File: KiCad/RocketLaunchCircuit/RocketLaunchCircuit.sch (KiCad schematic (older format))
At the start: 36 parts, among them J1 Arduino_GPIO, J10 LogicConverter_BiDirectional, J11 ConnectorTarget3, J12 ConnectorTarget4, J13 ExternalGameControlIO, J14 Dupont_3Pin_Female, J15 Screw_Terminal_01x02, J2 Arduino_Serial_And_5V, J3 MicroBit_40PinExtender, J4 ConnectorTarget1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

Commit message: Created a custom symbol for the bi-directional logic converter module
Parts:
- removed J10, J8: LogicConverter_BiDirectional, symbol Connector_Generic:Conn_02x06_Row_Letter_Last
- added U1, U2: Bi-Directional_logic_shifter, symbol RocketLaunch_Library:Bi-Directional_logic_shifter
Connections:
- wire segments 195 -> 199
- no-connect marks 0 -> 15
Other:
- note added: "Notch of the IDC connectors (see list) on this side:\n- Arduino_GPIO\n- Arduino_Serial_and_5V\n- MicroBit_40PinExtender"
- moved on the sheet: C5, C6, C7, C8, J13, J3, R5, R7, R8, R9

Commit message: Updated the names of the LedDataTargetx singals with the correct values for 'x'
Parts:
- C1, C2, C3, C4, C5, C6, C7, C8: symbol Device:C -> RocketLaunchCircuit-rescue:C-Device
- J1, J13: symbol Connector_Generic:Conn_02x05_Counter_Clockwise -> RocketLaunchCircuit-rescue:Conn_02x05_Counter_Clockwise-Connector_Generic
- J11, J12, J4, J7: symbol Connector_Generic:Conn_01x05 -> RocketLaunchCircuit-rescue:Conn_01x05-Connector_Generic
- J14, J9: symbol Connector_Generic:Conn_01x03 -> RocketLaunchCircuit-rescue:Conn_01x03-Connector_Generic
- J15: symbol Connector:Screw_Terminal_01x02 -> RocketLaunchCircuit-rescue:Screw_Terminal_01x02-Connector
- J2: symbol Connector_Generic:Conn_02x03_Counter_Clockwise -> RocketLaunchCircuit-rescue:Conn_02x03_Counter_Clockwise-Connector_Generic
- J3: symbol Connector_Generic:Conn_02x20_Row_Letter_Last -> RocketLaunchCircuit-rescue:Conn_02x20_Row_Letter_Last-Connector_Generic
- J5, J6: symbol Connector:USB_A -> RocketLaunchCircuit-rescue:USB_A-Connector
- R1, R2, R3, R4, R5, R7, R8, R9: symbol Device:R -> RocketLaunchCircuit-rescue:R-Device
- R6: symbol Device:R_Small -> RocketLaunchCircuit-rescue:R_Small-Device
- SW1: symbol Switch:SW_DPST_x2 -> RocketLaunchCircuit-rescue:SW_DPST_x2-Switch
- SW2, SW3: symbol Switch:SW_DPDT_x2 -> RocketLaunchCircuit-rescue:SW_DPDT_x2-Switch
- SW4: symbol Device:Rotary_Encoder_Switch -> RocketLaunchCircuit-rescue:Rotary_Encoder_Switch-Device
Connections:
- net LedDataTarget1_5V: no longer J11.3 (Pin_3), J12.3 (Pin_3), J7.3 (Pin_3)
- net LedDataTarget2_5V: now also J7.3 (Pin_3)
- net LedDataTarget3_5V: now also J11.3 (Pin_3)
- net LedDataTarget4_5V: now also J12.3 (Pin_3)
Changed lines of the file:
@@
 $EndDescr
 $Comp
-L Connector:Screw_Terminal_01x02 J15
+L RocketLaunchCircuit-rescue:Screw_Terminal_01x02-Connector J15
 U 1 1 5E6E483D
 P 6500 7150
@@
 $EndComp
 $Comp
-L Switch:SW_DPDT_x2 SW2
+L RocketLaunchCircuit-rescue:SW_DPDT_x2-Switch SW2
 U 1 1 5E6E85BB
 P 8500 2100
@@
 $EndComp
 $Comp
-L power:GND #PWR011
+L RocketLaunchCircuit-rescue:GND-power #PWR011
 U 1 1 5E707618
 P 2150 3300
@@
 5V_PowerSupply
 $Comp
-L Connector_Generic:Conn_01x03 J9
+L RocketLaunchCircuit-rescue:Conn_01x03-Connector_Generic J9
 U 1 1 5E6A9AF2
 P 4950 700
@@
 $EndComp
 $Comp
-L Connector_Generic:Conn_02x03_Counter_Clockwise J2
+L RocketLaunchCircuit-rescue:Conn_02x03_Counter_Clockwise-Connector_Generic J2
 U 1 1 5E6AB262
 P 3350 2300
@@
 $EndComp
 $Comp
-L Connector_Generic:Conn_02x05_Counter_Clockwise J1
+L RocketLaunchCircuit-rescue:Conn_02x05_Counter_Clockwise-Connector_Generic J1
 U 1 1 5E6AC440
 P 3500 1300
@@
 $EndComp
 $Comp
-L Connector_Generic:Conn_02x20_Row_Letter_Last J3
+L RocketLaunchCircuit-rescue:Conn_02x20_Row_Letter_Last-Connector_Generic J3
 U 1 1 5E6AC8BC
 P 3200 4950
@@
 	8300 2000 7950 2000
 $Comp
-L power:GND #PWR017
+L RocketLaunchCircuit-rescue:GND-power #PWR017
 U 1 1 5E6AFC6B
 P 8050 2200
@@
 PlayerCountSignal
 $Comp
-L Switch:SW_DPDT_x2 SW3
+L RocketLaunchCircuit-rescue:SW_DPDT_x2-Switch SW3
 U 1 1 5E6B920E
 P 8500 2850
@@
 	8300 2750 7950 2750
 $Comp
-L power:GND #PWR018
+L RocketLaunchCircuit-rescue:GND-power #PWR018
 U 1 1 5E6B9215
 P 8050 2950
@@
 LedMatrixData
 $Comp
-L power:GND #PWR07
+L RocketLaunchCircuit-rescue:GND-power #PWR07
 U 1 1 5E6CDC4C
 P 5050 1300
@@
 5V_PowerSupply
 $Comp
-L power:GND #PWR019
+L RocketLaunchCircuit-rescue:GND-power #PWR019
 U 1 1 5E73009E
 P 6300 6800
@@
 MicroBit_P16
 $Comp
-L power:GND #PWR021
+L RocketLaunchCircuit-rescue:GND-power #PWR021
 U 1 1 5E98B09B
 P 3500 4150
@@
 Arduino_5V
 $Comp
-L power:GND #PWR022
+L RocketLaunchCircuit-rescue:GND-power #PWR022
 U 1 1 5EBDEE77
 P 3700 2400
@@
 StartResetSignal
 $Comp
-L power:GND #PWR016
+L RocketLaunchCircuit-rescue:GND-power #PWR016
 U 1 1 5ED7A6E1
 P 8650 3450
@@
 $EndComp
 $Comp
-L Switch:SW_DPST_x2 SW1
+L RocketLaunchCircuit-rescue:SW_DPST_x2-Switch SW1
 U 1 1 5E6EA688
 P 8400 3450
@@
 	2100 3300 2150 3300
 $Comp
-L Connector:USB_A J5
+L RocketLaunchCircuit-rescue:USB_A-Connector J5
 U 1 1 5E70F829
 P 2100 2900
@@
 $EndComp
 $Comp
-L power:GND #PWR012
+L RocketLaunchCircuit-rescue:GND-power #PWR012
 U 1 1 5E77BF6C
 P 2750 3900
@@
 	2700 3900 2750 3900
 $Comp
-L Connector:USB_A J6
+L RocketLaunchCircuit-rescue:USB_A-Connector J6
 U 1 1 5E77BF75
 P 2700 3500
@@
 	3500 4050 3500 4150
 $Comp
-L Connector_Generic:Conn_01x05 J4
+L RocketLaunchCircuit-rescue:Conn_01x05-Connector_Generic J4
 U 1 1 5E7ECC5B
 P 2450 7150
@@
 $EndComp
 $Comp
-L power:GND #PWR02
+L RocketLaunchCircuit-rescue:GND-power #PWR02
 U 1 1 5E7EF8C8
 P 2750 6850
@@
 LedDataTarget1_5V
 $Comp
-L Device:R R1
+L RocketLaunchCircuit-rescue:R-Device R1
 U 1 1 5E7EF8D4
 P 2300 6500
@@
 $EndComp
 $Comp
-L Device:C C1
+L RocketLaunchCircuit-rescue:C-Device C1
 U 1 1 5E7EF8DA
 P 2050 6500
@@
 SwitchTarget1
 $Comp
-L power:GND #PWR01
+L RocketLaunchCircuit-rescue:GND-power #PWR01
 U 1 1 5E80F09C
 P 2100 6650
@@
 SizeTarget1
 $Comp
-L Connector_Generic:Conn_01x05 J7
+L RocketLaunchCircuit-rescue:Conn_01x05-Connector_Generic J7
 U 1 1 5E87FD51
 P 3500 7150
@@
 $EndComp
 $Comp
-L power:GND #PWR06
+L RocketLaunchCircuit-rescue:GND-power #PWR06
 U 1 1 5E87FD57
 P 3800 6850
@@
 	3500 6950 3500 6250
 Text Label 3500 6250 3    50   ~ 0
-LedDataTarget1_5V
-$Comp
-L Device:R R2
+LedDataTarget2_5V
+$Comp
+L RocketLaunchCircuit-rescue:R-Device R2
 U 1 1 5E87FD63
 P 3350 6500
@@
 $EndComp
 $Comp
-L Device:C C2
+L RocketLaunchCircuit-rescue:C-Device C2
 U 1 1 5E87FD69
 P 3100 6500
@@
 SwitchTarget2
 $Comp
-L power:GND #PWR03
+L RocketLaunchCircuit-rescue:GND-power #PWR03
 U 1 1 5E87FD71
 P 3150 6650
@@
 SizeTarget2
 $Comp
-L Connector_Generic:Conn_01x05 J11
+L RocketLaunchCircuit-rescue:Conn_01x05-Connector_Generic J11
 U 1 1 5E88B164
 P 4550 7150
@@
 $EndComp
 $Comp
-L power:GND #PWR013
+L RocketLaunchCircuit-rescue:GND-power #PWR013
 U 1 1 5E88B16A
 P 4850 6850
@@
 	4550 6950 4550 6250
 Text Label 4550 6250 3    50   ~ 0
-LedDataTarget1_5V
-$Comp
-L Device:R R3
+LedDataTarget3_5V
+$Comp
+L RocketLaunchCircuit-rescue:R-Device R3
 U 1 1 5E88B176
 P 4400 6500
@@
 $EndComp
 $Comp
-L Device:C C3
+L RocketLaunchCircuit-rescue:C-Device C3
 U 1 1 5E88B17C
 P 4150 6500
@@
 SwitchTarget3
 $Comp
-L power:GND #PWR010
+L RocketLaunchCircuit-rescue:GND-power #PWR010
 U 1 1 5E88B184
 P 4200 6650
@@
 SizeTarget3
 $Comp
-L Connector_Generic:Conn_01x05 J12
+L RocketLaunchCircuit-rescue:Conn_01x05-Connector_Generic J12
 U 1 1 5E897B46
 P 5600 7150
@@
 $EndComp
 $Comp
-L power:GND #PWR015
+L RocketLaunchCircuit-rescue:GND-power #PWR015
 U 1 1 5E897B4C
 P 5900 6850
@@
 	5600 6950 5600 6250
 Text Label 5600 6250 3    50   ~ 0
-LedDataTarget1_5V
-$Comp
-L Device:R R4
+LedDataTarget4_5V
+$Comp
+L RocketLaunchCircuit-rescue:R-Device R4
 U 1 1 5E897B58
 P 5450 6500
@@
 $EndComp
 $Comp
-L Device:C C4
+L RocketLaunchCircuit-rescue:C-Device C4
 U 1 1 5E897B5E
 P 5200 6500
@@
 SwitchTarget4
 $Comp
-L power:GND #PWR014
+L RocketLaunchCircuit-rescue:GND-power #PWR014
 U 1 1 5E897B66
 P 5250 6650
@@
 SizeTarget4
 $Comp
-L power:GND #PWR024
+L RocketLaunchCircuit-rescue:GND-power #PWR024
 U 1 1 5E8F3D2E
 P 8000 1400
@@
 PointSelectorEncoderB
 $Comp
-L power:GND #PWR025
+L RocketLaunchCircuit-rescue:GND-power #PWR025
 U 1 1 5E942130
 P 8700 1500
@@
 $EndComp
 $Comp
-L Device:Rotary_Encoder_Switch SW4
+L RocketLaunchCircuit-rescue:Rotary_Encoder_Switch-Device SW4
 U 1 1 5E8F157E
 P 8350 1400
@@
 	5600 1600 6000 1600
 $Comp
-L power:GND #PWR023
+L RocketLaunchCircuit-rescue:GND-power #PWR023
 U 1 1 5EB8702E
 P 5850 1900
@@
 	8750 2650 8750 2850
 $Comp
-L Connector_Generic:Conn_01x03 J14
+L RocketLaunchCircuit-rescue:Conn_01x03-Connector_Generic J14
 U 1 1 5EB538A7
 P 6200 1700
@@
 $EndComp
 $Comp
-L Device:R_Small R6
+L RocketLaunchCircuit-rescue:R_Small-Device R6
 U 1 1 5EB9F373
 P 5850 1800
@@
 	5200 3250 5200 3300
 $Comp
-L power:GND #PWR04
+L RocketLaunchCircuit-rescue:GND-power #PWR04
 U 1 1 5EA19618
 P 5300 3250
@@
 	5300 3250 5300 3300
 $Comp
-L power:GND #PWR05
+L RocketLaunchCircuit-rescue:GND-power #PWR05
 U 1 1 5EA3BCA6
 P 5300 4350
@@
 	5600 4700 5600 4750
 $Comp
-L power:GND #PWR08
+L RocketLaunchCircuit-rescue:GND-power #PWR08
 U 1 1 5EB84976
 P 5700 4700
@@
 	5700 4700 5700 4750
 $Comp
-L power:GND #PWR09
+L RocketLaunchCircuit-rescue:GND-power #PWR09
 U 1 1 5EB94E6F
 P 5700 5800
@@
 	4450 2750 4800 2750
 $Comp
-L Device:C C6
+L RocketLaunchCircuit-rescue:C-Device C6
 U 1 1 5EDDB888
 P 4450 2600
@@
 	4650 2950 4800 2950
 $Comp
-L Device:C C7
+L RocketLaunchCircuit-rescue:C-Device C7
 U 1 1 5ED5AEFD
 P 4550 2700
@@
 $EndComp
 $Comp
-L Device:C C8
+L RocketLaunchCircuit-rescue:C-Device C8
 U 1 1 5ED22825
 P 4650 2800
@@
 	6000 2750 6750 2750
 $Comp
-L Device:R R9
+L RocketLaunchCircuit-rescue:R-Device R9
 U 1 1 5ECBAF3A
 P 4950 2950
@@
 $EndComp
 $Comp
-L Device:R R8
+L RocketLaunchCircuit-rescue:R-Device R8
 U 1 1 5ECACC72
 P 4950 2850
@@
 $EndComp
 $Comp
-L Device:R R7
+L RocketLaunchCircuit-rescue:R-Device R7
 U 1 1 5EC9E8CF
 P 4950 2750
@@
 	5650 2950 6600 2950
 $Comp
-L power:GND #PWR020
+L RocketLaunchCircuit-rescue:GND-power #PWR020
 U 1 1 5E8DAE92
 P 6150 2450
@@
 $EndComp
 $Comp
-L Connector_Generic:Conn_02x05_Counter_Clockwise J13
+L RocketLaunchCircuit-rescue:Conn_02x05_Counter_Clockwise-Connector_Generic J13
 U 1 1 5E8CF06C
 P 5350 2750
@@
 $EndComp
 $Comp
-L Device:C C5
+L RocketLaunchCircuit-rescue:C-Device C5
 U 1 1 5ED5FABC
 P 6000 2600
@@
 $EndComp
 $Comp
-L Device:R R5
+L RocketLaunchCircuit-rescue:R-Device R5
 U 1 1 5ED5FAB6
 P 5850 2750

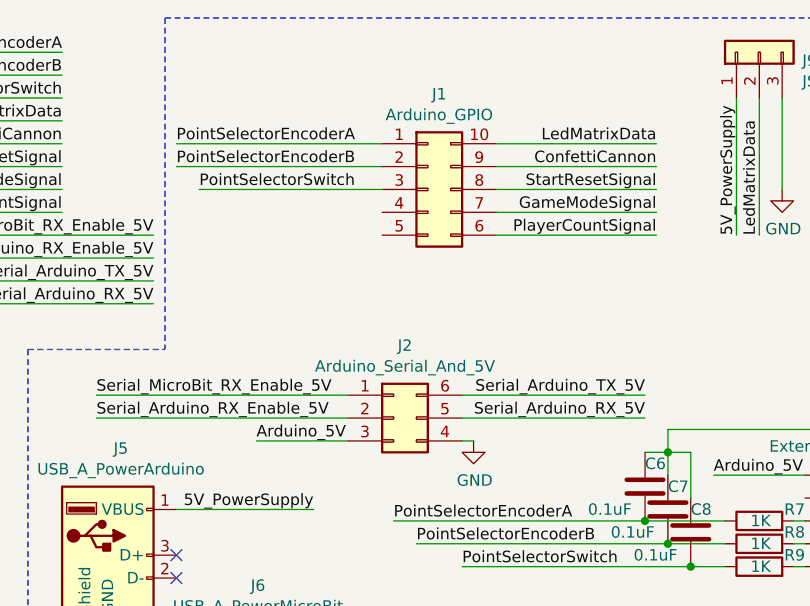
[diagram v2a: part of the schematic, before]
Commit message: Updated the connector pin layout for the idc connectors between the arduino and the perfboard
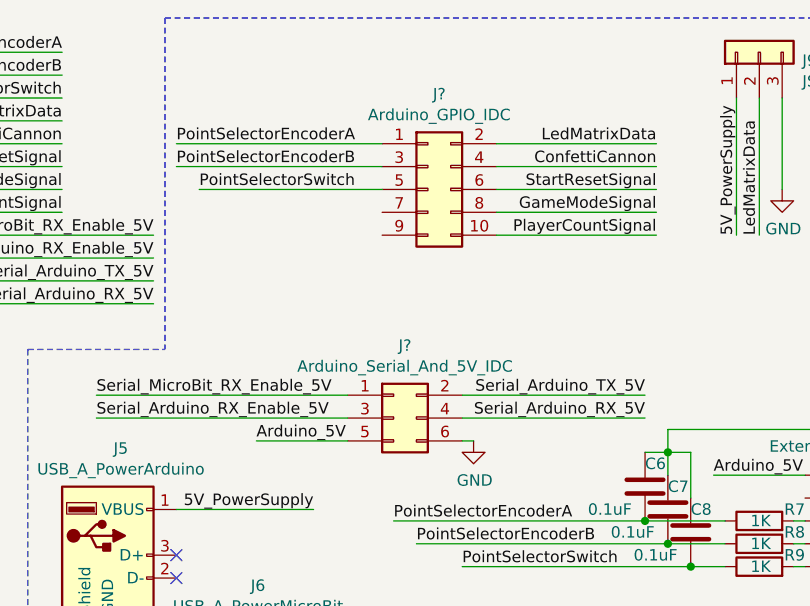
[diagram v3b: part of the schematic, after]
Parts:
- removed J1: Arduino_GPIO, symbol RocketLaunchCircuit-rescue:Conn_02x05_Counter_Clockwise-Connector_Generic
- removed J2: Arduino_Serial_And_5V, symbol RocketLaunchCircuit-rescue:Conn_02x03_Counter_Clockwise-Connector_Generic
- added J?: Arduino_GPIO_IDC, symbol Connector_Generic:Conn_02x05_Odd_Even
- added J?: Arduino_Serial_And_5V_IDC, symbol Connector_Generic:Conn_02x03_Odd_Even
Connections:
- net Arduino_5V: now also J?.5 (Pin_5)
- net Arduino_P0: now also J?.4 (Pin_4)
- net Arduino_P1: now also J?.2 (Pin_2)
- net Arduino_P10: now also J?.3 (Pin_3)
- net Arduino_P11: now also J?.1 (Pin_1)
- net Arduino_P2: now also J?.3 (Pin_3)
- net Arduino_P3: now also J?.1 (Pin_1)
- net Arduino_P4: now also J?.10 (Pin_10)
- net Arduino_P5: now also J?.8 (Pin_8)
- net Arduino_P6: now also J?.6 (Pin_6)
- net Arduino_P7: now also J?.4 (Pin_4)
- net Arduino_P8: now also J?.2 (Pin_2)
- net Arduino_P9: now also J?.5 (Pin_5)
- net GND: now also J?.6 (Pin_6)
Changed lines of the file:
@@
-$EndComp
-$Comp
-L RocketLaunchCircuit-rescue:Conn_02x03_Counter_Clockwise-Connector_Generic J2
-U 1 1 5E6AB262
-P 3350 2300
-F 0 "J2" H 3400 2617 50  0000 C CNN
-F 1 "Arduino_Serial_And_5V" H 3400 2526 50  0000 C CNN
-F 2 "" H 3350 2300 50  0001 C CNN
-F 3 "~" H 3350 2300 50  0001 C CNN
-	1    3350 2300
-	1    0    0    -1
-$EndComp
-$Comp
-L RocketLaunchCircuit-rescue:Conn_02x05_Counter_Clockwise-Connector_Generic J1
-U 1 1 5E6AC440
-P 3500 1300
-F 0 "J1" H 3550 1717 50  0000 C CNN
-F 1 "Arduino_GPIO" H 3550 1626 50  0000 C CNN
-F 2 "" H 3500 1300 50  0001 C CNN
-F 3 "~" H 3500 1300 50  0001 C CNN
-	1    3500 1300
-	1    0    0    -1
 $EndComp
 $Comp
@@
 Connection ~ 3500 4150
 Connection ~ 3500 4050
+$Comp
+L Connector_Generic:Conn_02x05_Odd_Even J?
+U 1 1 5EF161BD
+P 3500 1300
+F 0 "J?" H 3550 1717 50  0000 C CNN
+F 1 "Arduino_GPIO_IDC" H 3550 1626 50  0000 C CNN
+F 2 "" H 3500 1300 50  0001 C CNN
+F 3 "~" H 3500 1300 50  0001 C CNN
+	1    3500 1300
+	1    0    0    -1
+$EndComp
+$Comp
+L Connector_Generic:Conn_02x03_Odd_Even J?
+U 1 1 5EF1750E
+P 3350 2300
+F 0 "J?" H 3400 2617 50  0000 C CNN
+F 1 "Arduino_Serial_And_5V_IDC" H 3400 2526 50  0000 C CNN
+F 2 "" H 3350 2300 50  0001 C CNN
+F 3 "~" H 3350 2300 50  0001 C CNN
+	1    3350 2300
+	1    0    0    -1
+$EndComp
 $EndSCHEMATC

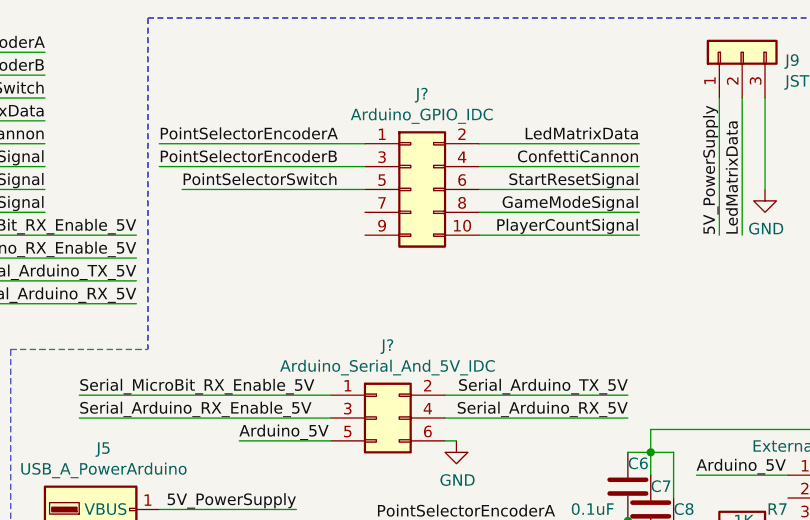
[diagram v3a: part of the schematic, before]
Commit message: Added the missing annotations to the connectors
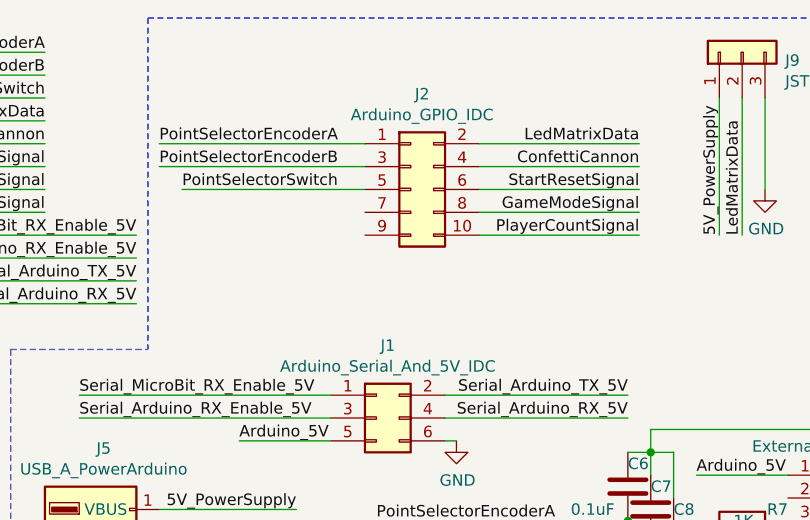
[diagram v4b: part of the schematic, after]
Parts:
- gave numbers to parts that had none: 2
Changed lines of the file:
@@
 Connection ~ 3500 4050
 $Comp
-L Connector_Generic:Conn_02x05_Odd_Even J?
+L Connector_Generic:Conn_02x05_Odd_Even J2
 U 1 1 5EF161BD
 P 3500 1300
-F 0 "J?" H 3550 1717 50  0000 C CNN
+F 0 "J2" H 3550 1717 50  0000 C CNN
 F 1 "Arduino_GPIO_IDC" H 3550 1626 50  0000 C CNN
 F 2 "" H 3500 1300 50  0001 C CNN
@@
 $EndComp
 $Comp
-L Connector_Generic:Conn_02x03_Odd_Even J?
+L Connector_Generic:Conn_02x03_Odd_Even J1
 U 1 1 5EF1750E
 P 3350 2300
-F 0 "J?" H 3400 2617 50  0000 C CNN
+F 0 "J1" H 3400 2617 50  0000 C CNN
 F 1 "Arduino_Serial_And_5V_IDC" H 3400 2526 50  0000 C CNN
 F 2 "" H 3350 2300 50  0001 C CNN

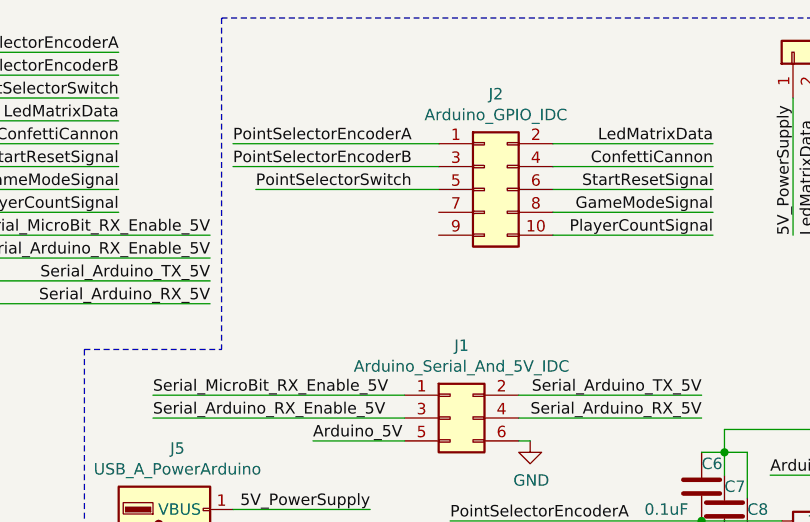
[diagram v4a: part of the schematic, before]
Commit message: Added 5V and GND to the Arduino_GPIO_IDC connector
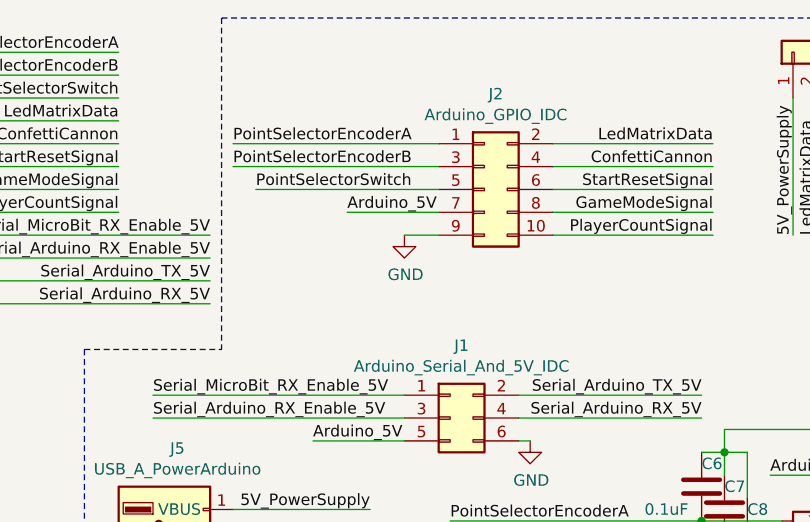
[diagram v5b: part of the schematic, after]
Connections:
- net Arduino_5V: now also J2.7 (Pin_7)
- net GND: now also J2.9 (Pin_9)
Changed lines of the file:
@@
 	1    0    0    -1
 $EndComp
+Wire Wire Line
+	2900 1400 3300 1400
+Text Label 2900 1400 0    50   ~ 0
+Arduino_5V
+$Comp
+L power:GND #PWR?
+U 1 1 5EF2356B
+P 3150 1500
+F 0 "#PWR?" H 3150 1250 50  0001 C CNN
+F 1 "GND" H 3155 1327 50  0000 C CNN
+F 2 "" H 3150 1500 50  0001 C CNN
+F 3 "" H 3150 1500 50  0001 C CNN
+	1    3150 1500
+	1    0    0    -1
+$EndComp
+Wire Wire Line
+	3150 1500 3300 1500
 $EndSCHEMATC
